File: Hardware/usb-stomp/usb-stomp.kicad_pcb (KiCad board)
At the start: 4 copper layers, 50 x 143 mm, 126 parts, among them J1 USB_C_Receptacle_USB2.0_16P, J2 Barrel_Jack_Switch, J301 AudioJack3_SwitchTR, J5 AudioJack4, J6 AudioJack4, J7 AudioJack3_SwitchTR, J8 I2C1, SW1 SW_SPST, SW101 RotaryEncoder_Switch_MP, SW102 RotaryEncoder_Switch_MP, U1 TLV76733DRVx, U103 TLV76733DRVx, U2 TLV76750DRVx, U201 74AHCT2G125, U3 USBLC6-2P6, U301 OPA2365AIDR, U302 TAC5242, U4 TLP2310, U401 RP2354A, U6 M24C64-FMH6TG, Y401 ABM8-272-T3

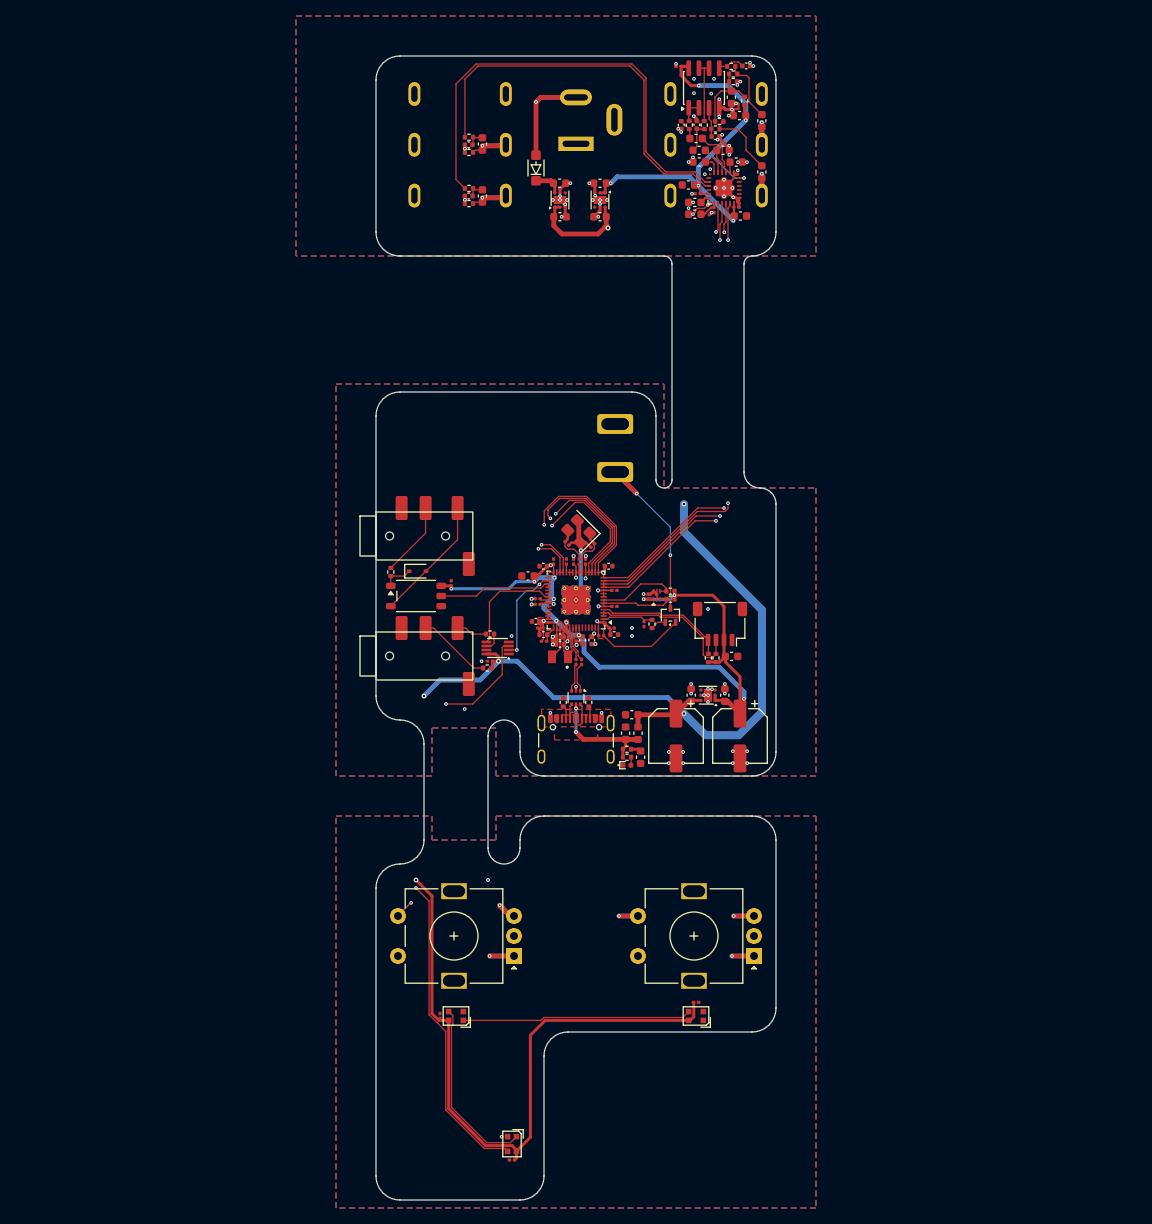
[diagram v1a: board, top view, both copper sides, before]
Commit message: Let's re-do the usb-stomp board without the flex board
It was a teaching experience, but I guess the lesson was "don't do
that".  Let's just turn it into a straightforward simple single board.

I did decide to try a buck regulator, and I'm also playing with adding
support for a remote stomp switch or expression pedal.  I'm trying to do
it in a way that pretty much anything could be made to work - a single
remote stomp over a TS 1/4" cable, or a dual remote stomp over a TRS
one.  Or an expression pedal. But maybe I screwed that thing up.

The TRS Typa-A midi ports remain for remote control, but I'm thinking
that it shouldn't be too hard to teach WebMIDI to set up a model where
the remote stomp / expression pedal can control some arbitrary pot
value in the scene.

There's also a rotary encoder for the same reason - program the scene to
make it be the master volume, or the noise gate level, or whatever.

Of course, that "program the scene" part is all just a nebulous plan.  I
don't actually support that yet.  SMOP.

Signed-off-by: Linus Torvalds <torvalds@linux-foundation.org>
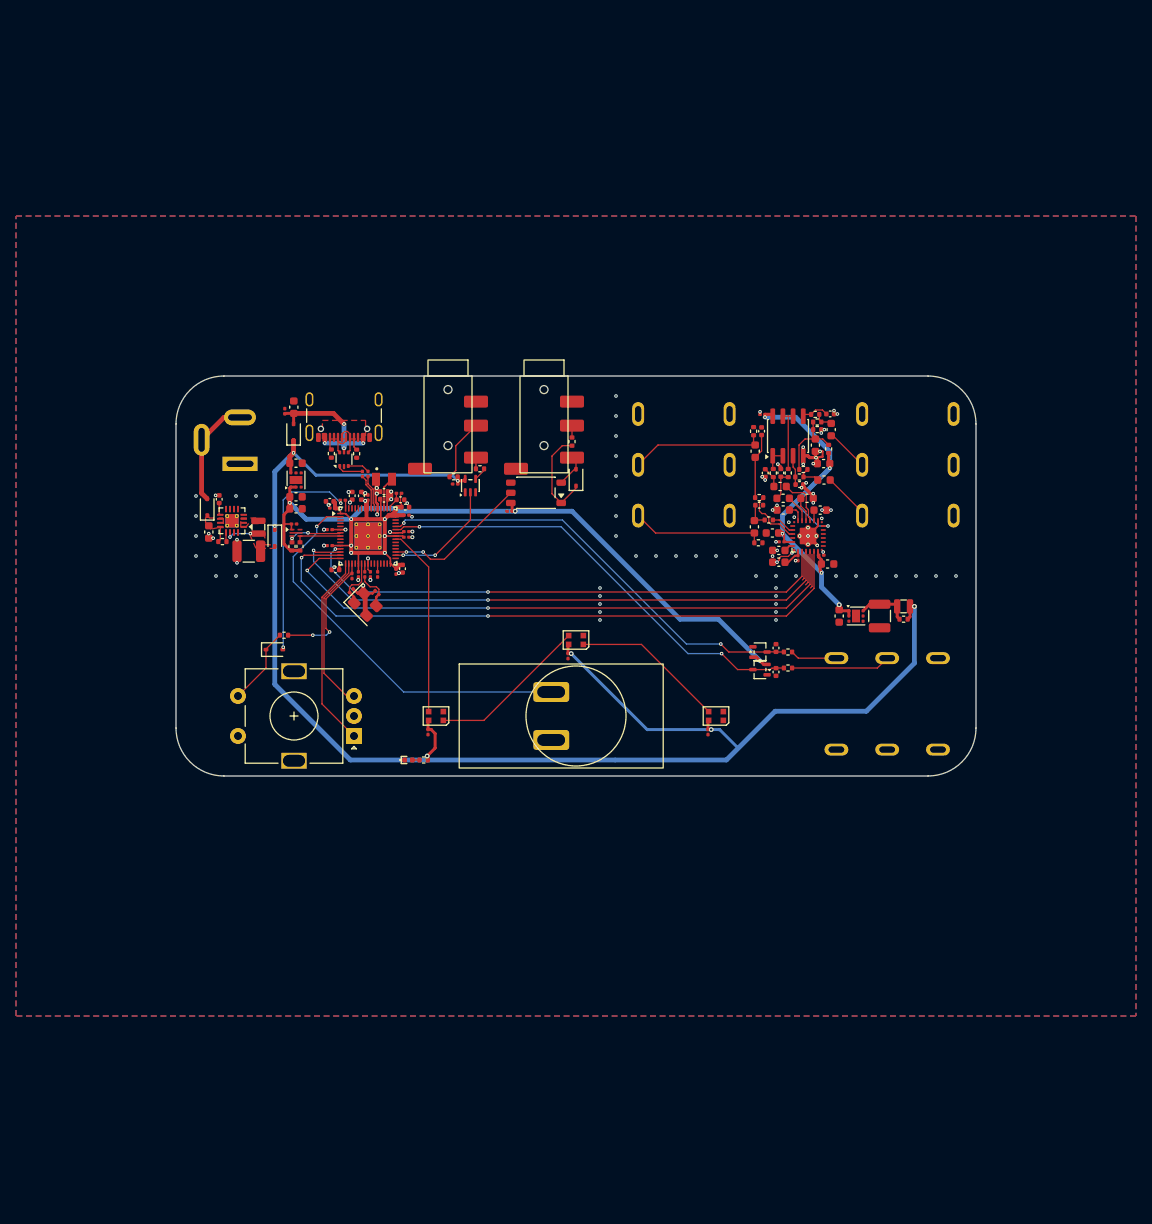
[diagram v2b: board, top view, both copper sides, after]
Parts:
- removed C1, C126, C127, C14, C2, C3, C4, C5, C6, C7: 2.2uF, Capacitor_SMD:C_0603_1608Metric
- removed C10, C11, C128, C15: 0.1uF, Capacitor_SMD:C_0201_0603Metric
- removed C12, C13: 47uF, Capacitor_SMD:CP_Elec_6.3x5.9
- removed C8: 10uF, Capacitor_SMD:C_0603_1608Metric
- removed D1: SM4007PL, Mylib:SOD-123FL
- removed D2: LED, LED_SMD:LED_0402_1005Metric
- removed D3: 1N4148WS, Diode_SMD:D_SOD-323
- removed FB1: BLM18PG, Inductor_SMD:L_0603_1608Metric
- removed J1: USB_C_Receptacle_USB2.0_16P, Connector_USB:USB_C_Receptacle_GCT_USB4105-xx-A_16P_TopMnt_Horizontal
- removed J2: Barrel_Jack_Switch, Mylib:Wurth WR-DC 2.1mm Power Jack
- removed J5, J6: AudioJack4, Mylib:PJ-320D
- removed J7: AudioJack3_SwitchTR, Mylib:NRJ6HM-1-PRE
- removed J8: I2C1, Connector_JST:JST_SH_SM04B-SRSS-TB_1x04-1MP_P1.00mm_Horizontal
- removed R1, R2, R8, R9: 5k1, Resistor_SMD:R_0402_1005Metric
- removed R113, R4: 1k, Resistor_SMD:R_0402_1005Metric
- removed R3: 1R, Resistor_SMD:R_0402_1005Metric
- removed R5, R6, R7: 220, Resistor_SMD:R_0402_1005Metric
- removed SW1: SW_SPST, Mylib:Daier PBS-24B-2
- removed U1: TLV76733DRVx, Package_SON:WSON-6-1EP_2x2mm_P0.65mm_EP1x1.6mm
- removed U2: TLV76750DRVx, Package_SON:WSON-6-1EP_2x2mm_P0.65mm_EP1x1.6mm
- removed U3: USBLC6-2P6, Package_TO_SOT_SMD:SOT-666
- removed U4: TLP2310, Package_SO:SO-5-6_4.55x3.7mm_P1.27mm
- removed U6: M24C64-FMH6TG, Mylib:UFDFPN5
- added C105: 22nF, Capacitor_SMD:C_0402_1005Metric, F.Cu at (125.0, 107.0)
- added C106: 22uF, Capacitor_SMD:C_1210_3225Metric, F.Cu at (59.1, 91.9)
- added C107: 2.2nF, Capacitor_SMD:C_0402_1005Metric, F.Cu at (55.4, 85.4)
- added C108: 22nF, Capacitor_SMD:C_0402_1005Metric, F.Cu at (125.0, 104.0)
- added C109: 2.2uF, Capacitor_SMD:C_0603_1608Metric, F.Cu at (65.0, 80.9)
- added C110: 2.2uF, Capacitor_SMD:C_0603_1608Metric, F.Cu at (65.0, 86.6)
- added C111: 0.1uF, Capacitor_SMD:C_0201_0603Metric, F.Cu at (72.0, 95.0)
- added C112: 2.2uF, Capacitor_SMD:C_0603_1608Metric, F.Cu at (65.0, 85.1)
- added C204: 0.1uF, Capacitor_SMD:C_0201_0603Metric, F.Cu at (81.5, 114.5)
- added C205: 0.1uF, Capacitor_SMD:C_0201_0603Metric, F.Cu at (116.5, 114.5)
- added C322: 2.2uF, Capacitor_SMD:C_0603_1608Metric, F.Cu at (130.5, 86.8)
- added C323: 0.1uF, Capacitor_SMD:C_0201_0603Metric, F.Cu at (127.8, 92.8)
- added C324: 10uF, Capacitor_SMD:C_0603_1608Metric, F.Cu at (124.5, 89.6)
- added C325: 10uF, Capacitor_SMD:C_0603_1608Metric, F.Cu at (130.9, 81.0)
- added C326: 0.1uF, Capacitor_SMD:C_0201_0603Metric, F.Cu at (130.7, 92.4)
- added C327: 0.1uF, Capacitor_SMD:C_0201_0603Metric, F.Cu at (125.7, 90.7)
- added D104: 1N5819WS, Diode_SMD:D_SOD-323, F.Cu at (62.4, 90.2)
- added D105: BAT54SW, Package_TO_SOT_SMD:SOT-323_SC-70, F.Cu at (123.0, 106.7)
- added D106: 1N5819WS, Diode_SMD:D_SOD-323, F.Cu at (62.3, 104.2)
- added D107: BAT54SW, Package_TO_SOT_SMD:SOT-323_SC-70, F.Cu at (123.0, 104.5)
- added D202: WS2812B-2020-V6, LED_SMD:LED_WS2812B-2020_PLCC4_2.0x2.0mm, F.Cu at (82.5, 112.5)
- added D203: WS2812B-2020-V6, LED_SMD:LED_WS2812B-2020_PLCC4_2.0x2.0mm, F.Cu at (100.0, 103.0)
- added D204: WS2812B-2020-V6, LED_SMD:LED_WS2812B-2020_PLCC4_2.0x2.0mm, F.Cu at (117.5, 112.5)
- added J101: USB_C_Receptacle_USB2.0_16P, Connector_USB:USB_C_Receptacle_GCT_USB4105-xx-A_16P_TopMnt_Horizontal, F.Cu at (71.0, 74.0)
- added J102: Barrel_Jack_Switch, Mylib:Wurth WR-DC 2.1mm Power Jack, F.Cu at (58.0, 81.0)
- added J103: AudioJack3_SwitchTR, Mylib:NRJ6HM-1-PRE, F.Cu at (150.0, 112.5)
- added J201: AudioJack4, Mylib:PJ-320D, F.Cu at (96.0, 70.0)
- added J202: AudioJack4, Mylib:PJ-320D, F.Cu at (84.0, 70.0)
- added J302: AudioJack3_SwitchTR, Mylib:NRJ6HM-1-PRE, F.Cu at (143.0, 70.0)
- added L101: 2.2uH, Mylib:L_0806, F.Cu at (60.3, 88.9)
- added L301: 2.2uH, Mylib:L_0806, F.Cu at (140.9, 98.8)
- added R107: 1k, Resistor_SMD:R_0402_1005Metric, F.Cu at (126.5, 104.5)
- added R108: 100k, Resistor_SMD:R_0402_1005Metric, F.Cu at (55.8, 90.7)
- added R109: 1k, Resistor_SMD:R_0402_1005Metric, F.Cu at (63.5, 102.4)
- added R201: 220, Resistor_SMD:R_0402_1005Metric, F.Cu at (99.5, 78.2)
- added R202: 220, Resistor_SMD:R_0402_1005Metric, F.Cu at (84.7, 82.6)
- added R203: 220, Resistor_SMD:R_0402_1005Metric, F.Cu at (88.0, 81.6)
- added R309: 1k, Resistor_SMD:R_0402_1005Metric, F.Cu at (122.9, 85.2)
- added R310: 1MEG, Resistor_SMD:R_0402_1005Metric, F.Cu at (122.2, 76.9)
- added R311: 100R, Resistor_SMD:R_0402_1005Metric, F.Cu at (124.7, 82.1)
- added R312: 100R, Resistor_SMD:R_0402_1005Metric, F.Cu at (126.5, 82.1)
- added R313: 1R, Resistor_SMD:R_0402_1005Metric, F.Cu at (140.9, 100.4)
- added U101: USBLC6-2P6, Package_TO_SOT_SMD:SOT-666, F.Cu at (71.0, 80.4)
- added U102: M24C64-FMH6TG, Mylib:UFDFPN5, F.Cu at (65.0, 89.6)
- added U104: TLV76733DRVx, Package_SON:WSON-6-1EP_2x2mm_P0.65mm_EP1x1.6mm, F.Cu at (65.0, 83.0)
- added U202: TLP2310, Package_SO:SO-5-6_4.55x3.7mm_P1.27mm, F.Cu at (95.0, 84.6)
- added U303: TAC5242, Mylib:TAC5242, F.Cu at (129.0, 90.0)
- C101: value 2.2nF -> 0.1uF; footprint Capacitor_SMD:C_0402_1005Metric -> Capacitor_SMD:C_0201_0603Metric
- C102: value 2.2nF -> 10uF; footprint Capacitor_SMD:C_0402_1005Metric -> Capacitor_SMD:C_0603_1608Metric
- C103: value 2.2uF -> 0.1uF; footprint Capacitor_SMD:C_0603_1608Metric -> Capacitor_SMD:C_0201_0603Metric
- C104: value 2.2uF -> 10uF
- C304: value 0.1uF -> 2.2nF; footprint Capacitor_SMD:C_0201_0603Metric -> Capacitor_SMD:C_0402_1005Metric
- C305: value 150pF -> 2.2uF; footprint Capacitor_SMD:C_0402_1005Metric -> Capacitor_SMD:C_0603_1608Metric
- C306: value 150pF -> 0.1uF; footprint Capacitor_SMD:C_0402_1005Metric -> Capacitor_SMD:C_0201_0603Metric
- C307, C308: value 2.2nF -> 150pF
- C309, C311, C312: value 2.2uF -> 2.2nF; footprint Capacitor_SMD:C_0603_1608Metric -> Capacitor_SMD:C_0402_1005Metric
- C313, C314, C318: value 10uF -> 2.2uF
- C317: value 0.1uF -> 22uF; footprint Capacitor_SMD:C_0201_0603Metric -> Capacitor_SMD:C_1210_3225Metric
- C320: value 0.1uF -> 10uF; footprint Capacitor_SMD:C_0201_0603Metric -> Capacitor_SMD:C_0603_1608Metric
- C321: value 0.1uF -> 2.2uF; footprint Capacitor_SMD:C_0201_0603Metric -> Capacitor_SMD:C_0603_1608Metric
- D101: value BAT54CW -> 1N5819WS; footprint Package_TO_SOT_SMD:SOT-323_SC-70 -> Diode_SMD:D_SOD-323
- D102: value WS2812B-2020-V6 -> LED; footprint LED_SMD:LED_WS2812B-2020_PLCC4_2.0x2.0mm -> LED_SMD:LED_0402_1005Metric
- D103, D201: value WS2812B-2020-V6 -> 1N5819WS; footprint LED_SMD:LED_WS2812B-2020_PLCC4_2.0x2.0mm -> Diode_SMD:D_SOD-323
- J301: moved to F.Cu
- R101, R102: value 1k -> 5k1
- R103, R303: value 1MEG -> 1k
- R104: value 1MEG -> 5k1
- R106: value 5k1 -> 1k
- R305, R306: value 100R -> 1MEG
- SW101: value RotaryEncoder_Switch_MP -> SW_SPST; footprint Rotary_Encoder:RotaryEncoder_Alps_EC11E-Switch_Vertical_H20mm -> Mylib:Daier PBS-24B-2
- U103: value TLV76733DRVx -> TPS62153; footprint Package_SON:WSON-6-1EP_2x2mm_P0.65mm_EP1x1.6mm -> Package_DFN_QFN:VQFN-16-1EP_3x3mm_P0.5mm_EP1.68x1.68mm_ThermalVias
- U201: value 74AHCT2G125 -> SN74AHCT1G125DCKR; footprint Package_SO:VSSOP-8_2.3x2mm_P0.5mm -> Package_TO_SOT_SMD:SOT-353_SC-70-5
- U302: value TAC5242 -> TLV76733DRVx; footprint Mylib:TAC5242 -> Package_SON:WSON-6-1EP_2x2mm_P0.65mm_EP1x1.6mm
- moved C201 84.8 mm to (84.9, 83.5)
- moved D103 70.8 mm to (53.9, 86.4), turned to 90 degrees
- moved R103 69.8 mm to (81.0, 118.0), turned to 0 degrees
- moved D201 69.0 mm to (100.0, 82.7), turned to 90 degrees
- moved C202 63.7 mm to (91.7, 86.9), turned to 0 degrees
- moved U103 61.0 mm to (57.0, 88.1), turned to 180 degrees
- moved R306 59.6 mm to (122.8, 90.8), turned to 0 degrees
- moved C104 59.3 mm to (54.1, 89.5)
- moved C319 57.1 mm to (131.4, 93.5), turned to 0 degrees
- moved C318 57.1 mm to (132.9, 100.0), turned to -90 degrees
- moved SW102 57.1 mm to (72.2, 115.0)
- moved U302 56.0 mm to (135.0, 100.0), turned to 0 degrees
- moved C304 55.8 mm to (122.9, 86.2), turned to 180 degrees
- moved C317 54.8 mm to (137.9, 100.0)
- moved R104 54.0 mm to (64.5, 91.3), turned to -90 degrees
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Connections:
- C101 pad 2: Net-(C101-Pad2) -> VBUS
- C102 pad 1: GND -> VBUS
- C102 pad 2: Net-(C102-Pad2) -> GND
- C103 pad 1: Net-(C101-Pad2) -> +3V3
- C103 pad 2: /OUT^{LEFT} -> GND
- C104 pad 1: Net-(C102-Pad2) -> +9V
- C104 pad 2: /OUT^{RIGHT} -> GND
- C202 pad 2: +5V -> +3V3
- C304 pad 2: +3.3VA -> Net-(C304-Pad2)
- C305 pad 1: Net-(U301A-+) -> Net-(C304-Pad2)
- C305 pad 2: GND -> /TAC5242/OUT^{LEFT}
- C306 pad 1: Net-(U301B-+) -> GND
- C306 pad 2: GND -> +3.3VA
- C307 pad 1: GND -> Net-(U301A-+)
- C307 pad 2: Net-(C307-Pad2) -> GND
- C308 pad 1: GND -> Net-(U301B-+)
- C308 pad 2: Net-(C308-Pad2) -> GND
- C309 pad 1: Net-(C307-Pad2) -> GND
- C309 pad 2: /TAC5242/IN1P -> Net-(C309-Pad2)
- C310 pad 1: GND -> Net-(C309-Pad2)
- C310 pad 2: /TAC5242/IN1M -> /TAC5242/OUT^{RIGHT}
- C311 pad 1: Net-(C308-Pad2) -> GND
- C311 pad 2: /TAC5242/IN2P -> Net-(C311-Pad2)
- C312 pad 2: /TAC5242/IN2M -> Net-(C312-Pad2)
- C313 pad 1: +3.3VA -> Net-(C311-Pad2)
- C313 pad 2: GND -> /TAC5242/IN1P
- C314 pad 1: /TAC5242/DREG -> GND
- C314 pad 2: GND -> /TAC5242/IN1M
- C315 pad 1: /TAC5242/VREF -> Net-(C312-Pad2)
- C315 pad 2: GND -> /TAC5242/IN2P
- C316 pad 1: /TAC5242/MICBIAS -> GND
- C316 pad 2: GND -> /TAC5242/IN2M
- C317 pad 1: /TAC5242/DREG -> Net-(U302-IN)
- C320 pad 1: +3.3VA -> /TAC5242/DREG
- C321 pad 1: +3.3VA -> /TAC5242/VREF
- D101 pad 1: Net-(D101-Pad1) -> +5V
- D101 pad 2: /BOOTSEL -> VBUS
- D102 pad 1: Net-(D102-DOUT) -> GND
- D102 pad 2: GND -> Net-(D102-A)
- D103 pad 1: Net-(D103-DOUT) -> +9V
- D103 pad 2: GND -> Net-(D103-A)
- D201 pad 1: unconnected-(D201-DOUT-Pad1) -> Net-(D201-K)
- D201 pad 2: GND -> Net-(D201-A)
- J301 pad R: /TAC5242/IN^{RIGHT} -> /TAC5242/OUT^{RIGHT}
- J301 pad RN: GND -> unconnected-(J301-PadRN)
- J301 pad T: /TAC5242/IN^{LEFT} -> /TAC5242/OUT^{LEFT}
- J301 pad TN: GND -> unconnected-(J301-PadTN)
- R101 pad 1: /OUT1P -> Net-(J101-CC1)
- R101 pad 2: Net-(C101-Pad2) -> GND
- R102 pad 1: /OUT2P -> Net-(J101-CC2)
- R102 pad 2: Net-(C102-Pad2) -> GND
- R103 pad 1: /OUT^{LEFT} -> Net-(D102-A)
- R103 pad 2: GND -> +5V
- R104 pad 1: /OUT^{RIGHT} -> /RP2354/GPIO4
- R104 pad 2: GND -> +3V3
- R105 pad 1: /RP2354/GPIO4 -> /RP2354/GPIO5
- R106 pad 1: /RP2354/GPIO5 -> /RP2354/ADC0
- R106 pad 2: +3V3 -> /EXP_R
- R303 pad 1: Net-(C301-Pad2) -> /OUT1P
- R303 pad 2: Net-(C302-Pad2) -> Net-(C304-Pad2)
- R304 pad 1: Net-(C303-Pad2) -> Net-(C301-Pad2)
- R304 pad 2: Net-(C301-Pad2) -> Net-(C302-Pad2)
- R305 pad 1: Net-(C302-Pad2) -> Net-(C303-Pad2)
- R305 pad 2: Net-(U301A-+) -> Net-(C301-Pad2)
- R306 pad 1: Net-(C303-Pad2) -> /TAC5242/OUT^{LEFT}
- R306 pad 2: Net-(U301B-+) -> GND
- R307 pad 1: Net-(U301A--) -> Net-(C302-Pad2)
- R307 pad 2: Net-(C307-Pad2) -> Net-(U301A-+)
- R308 pad 1: Net-(U301B--) -> Net-(C303-Pad2)
- R308 pad 2: Net-(C308-Pad2) -> Net-(U301B-+)
- SW102 pad A: /RP2354/GPIO15 -> /RP2354/GPIO12
- SW102 pad B: /RP2354/GPIO16 -> /RP2354/GPIO13
- SW102 pad S1: /RP2354/GPIO17 -> Net-(D106-K)
- U103 pad 1: +3.3VA -> /SW
- U103 pad 2: +3.3VA -> /SW
- U103 pad 3: GND -> /SW
- U103 pad 6: +5V -> GND
- U201 pad 3: Net-(D102-DIN) -> GND
- U201 pad 4: GND -> Net-(R203-Pad1)
- U201 pad 5: /RP2354/GPIO25 -> +5V
- U302 pad 1: /TAC5242/DREG -> +3.3VA
- U302 pad 2: /RP2354/GPIO8 -> +3.3VA
- U302 pad 3: /RP2354/GPIO9 -> GND
- U302 pad 4: /RP2354/GPIO11 -> unconnected-(U302-EN-Pad4)
- U302 pad 5: /RP2354/GPIO10 -> GND
- U302 pad 6: +3.3VA -> Net-(U302-IN)
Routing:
- net GND: track 177.1 -> 50.4 mm, vias 94 -> 102
- net /RP2354/GPIO15: track 110.5 -> 0.00 mm, vias 2 -> 0
- net /RP2354/GPIO16: track 95.5 -> 0.00 mm, vias 2 -> 0
- net Net-(D102-DIN): track 77.3 -> 0.00 mm, vias 2 -> 0
- net /RP2354/GPIO17: track 77.0 -> 0.00 mm, vias 2 -> 0
- net /RP2354/GPIO12: track 92.7 -> 24.4 mm, vias 2 -> 0
- net /RP2354/GPIO14: track 82.0 -> 15.4 mm
- net +5V: track 257.2 -> 191.8 mm, vias 6 -> 7
- net /RP2354/GPIO13: track 82.3 -> 19.9 mm, vias 2 -> 0
- net /RP2354/ADC0: track 0.00 -> 56.2 mm, vias 0 -> 2
- net /RP2354/ADC1: track 0.00 -> 55.8 mm, vias 0 -> 2
- net /OUT1P: track 57.7 -> 3.01 mm
- net /RP2354/GPIO0: track 6.33 -> 49.5 mm, vias 0 -> 1
- net /OUT2P: track 50.1 -> 7.57 mm
- net +3V3: track 115.0 -> 155.2 mm, vias 15 -> 14
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- added copper zone on F.Cu, net +9V
- added copper zone on F.Cu, net /SW
- added copper zone on F.Cu, net /VOS
- removed copper zone on F.Cu, net +1V1
- removed copper zone on In2.Cu, net +1V1
- removed copper zone on F.Cu, net +3V3
- removed copper zone on In1.Cu, net +3V3
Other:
- board size 50 x 143 mm -> 100 x 50 mm
- board text removed: "MIDI IN"
- board text removed: "MIDI OUT"

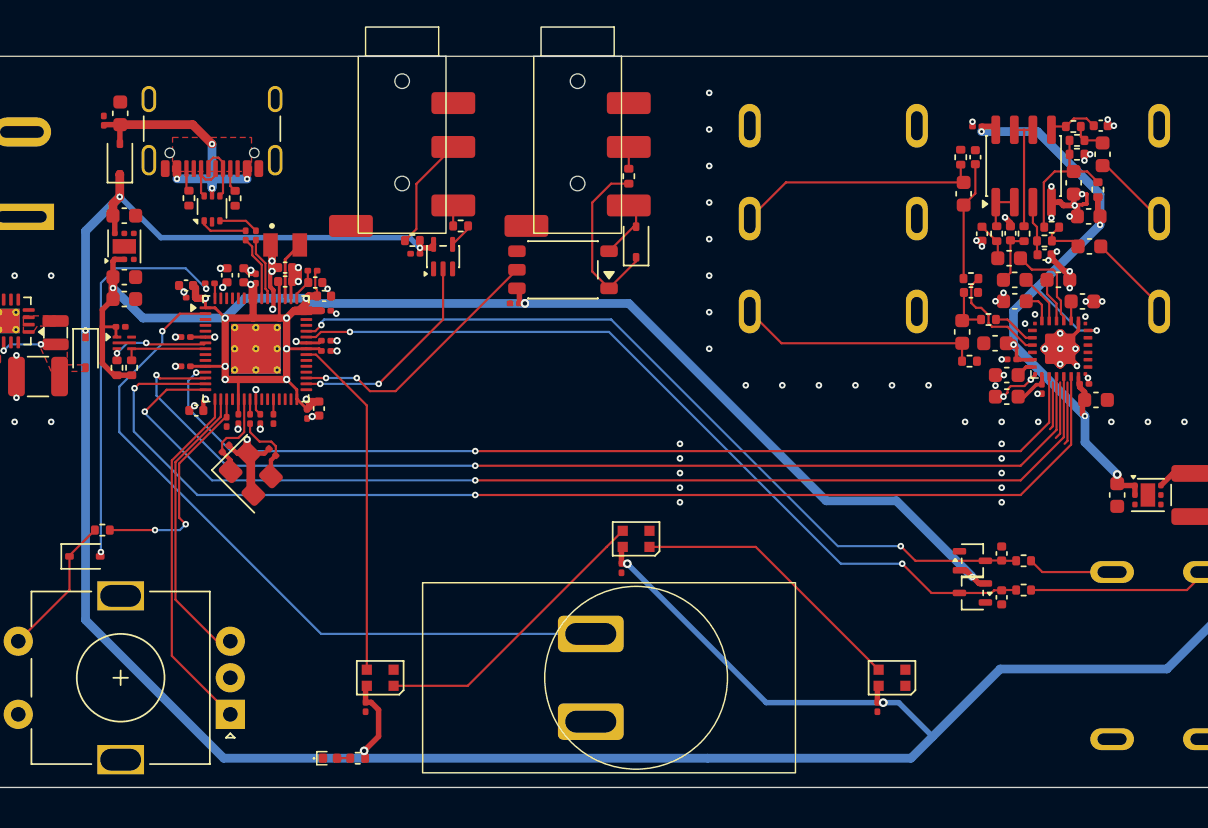
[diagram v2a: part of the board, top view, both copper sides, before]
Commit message: Partial re-route from component changes
Only the audio path for the larger input caps to the codec. MCU part comes next.

Signed-off-by: Linus Torvalds <torvalds@linux-foundation.org>
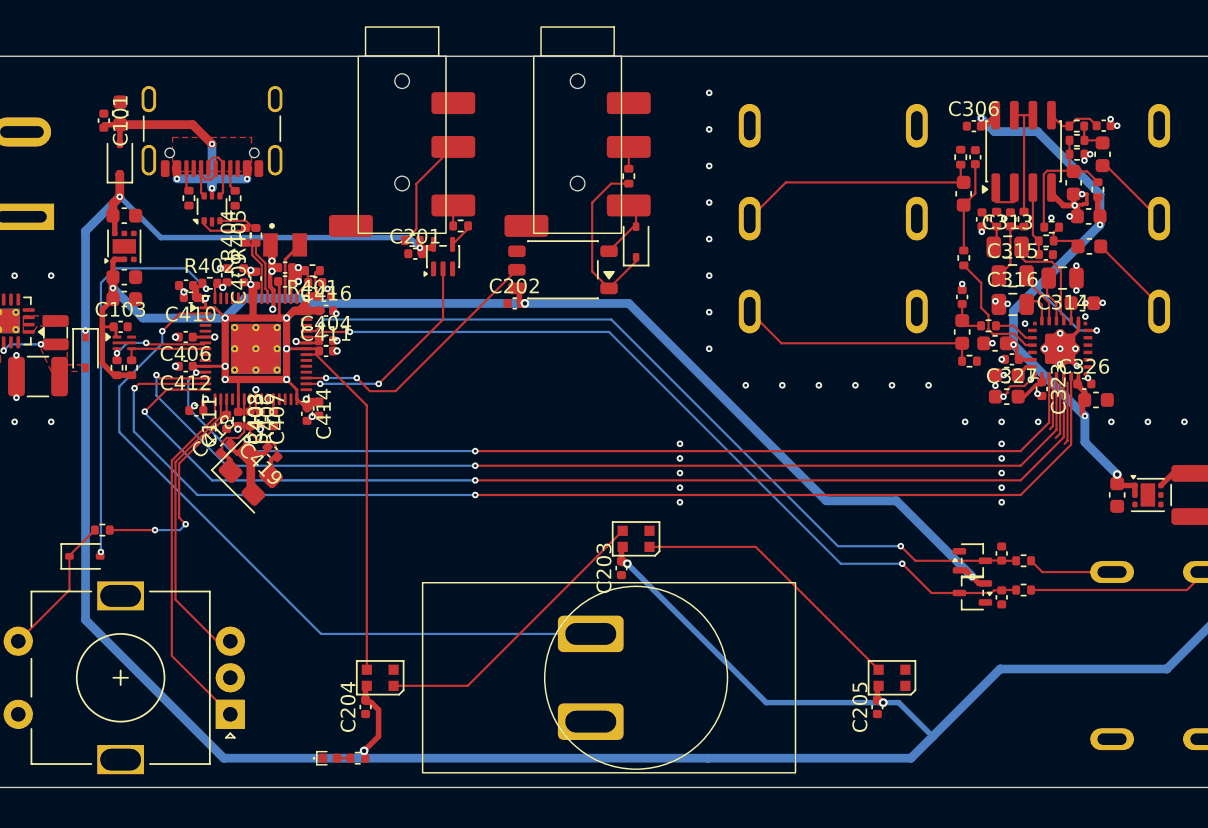
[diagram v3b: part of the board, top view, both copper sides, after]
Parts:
- C101, C103, C111, C201, C202, C203, C204, C205, C306, C323, C326, C327, C404, C406, C407, C408, C409, C410, C411, C412, C414, C416, C418, C419: footprint Capacitor_SMD:C_0201_0603Metric -> Capacitor_SMD:C_0402_1005Metric
- C313, C314, C315, C316: value 2.2uF -> 4.7uF; footprint Capacitor_SMD:C_0603_1608Metric -> Capacitor_SMD:C_0805_2012Metric
- R401, R404, R405: value 33R -> 33Ω; footprint Resistor_SMD:R_0201_0603Metric -> Resistor_SMD:R_0402_1005Metric
- R402, R403, R406: value 1k -> 1kΩ; footprint Resistor_SMD:R_0201_0603Metric -> Resistor_SMD:R_0402_1005Metric
- moved R309 1.49 mm to (122.4, 83.8), turned to 90 degrees
- moved U301 1.00 mm to (126.5, 76.5)
- moved R311 1.00 mm to (124.7, 81.1)
- moved R312 1.00 mm to (126.5, 81.1)
- moved C311 0.98 mm to (123.7, 81.2)
- moved C312 0.95 mm to (125.6, 81.2)
- moved C313 0.77 mm to (125.4, 83.0)
- moved C304 0.68 mm to (122.3, 86.5), turned to -90 degrees
- moved R303 0.43 mm to (124.1, 88.4)
- moved C315 0.31 mm to (125.8, 85.0)
- moved C314 0.31 mm to (129.2, 85.2)
- moved C316 0.26 mm to (125.8, 87.0)
- moved R308 0.24 mm to (130.1, 74.8)
- moved C306 0.23 mm to (123.1, 74.8)
- moved C308 0.20 mm to (132.0, 74.7)
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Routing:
- net GND: track 50.4 -> 47.1 mm, vias 102 -> 98
- net Net-(C309-Pad2): track 8.16 -> 6.24 mm
- net Net-(U301A--): track 2.94 -> 1.27 mm
- net Net-(U301A-+): track 3.73 -> 4.76 mm
- net /OUT2P: track 7.57 -> 8.52 mm
- net /TAC5242/IN1P: track 6.37 -> 7.30 mm
- net +3.3VA: track 51.6 -> 52.5 mm
- net Net-(C312-Pad2): track 3.86 -> 4.64 mm
- net Net-(C311-Pad2): track 2.53 -> 3.09 mm
